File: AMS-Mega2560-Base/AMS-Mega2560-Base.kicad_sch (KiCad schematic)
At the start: 18 parts, among them J1 RTD1, J2 RTD2, J3 AdafruitUltimateGPS, J4 Sense, J5 Sense, P1 Power, P10 CONN_01X01, P11 CONN_01X01, P12 CONN_01X01, P13 CONN_01X01, P2 Analog, P3 Analog, P4 Digital, P5 PWM, P6 PWM, P7 Communication, P8 CONN_01X01, P9 CONN_01X01

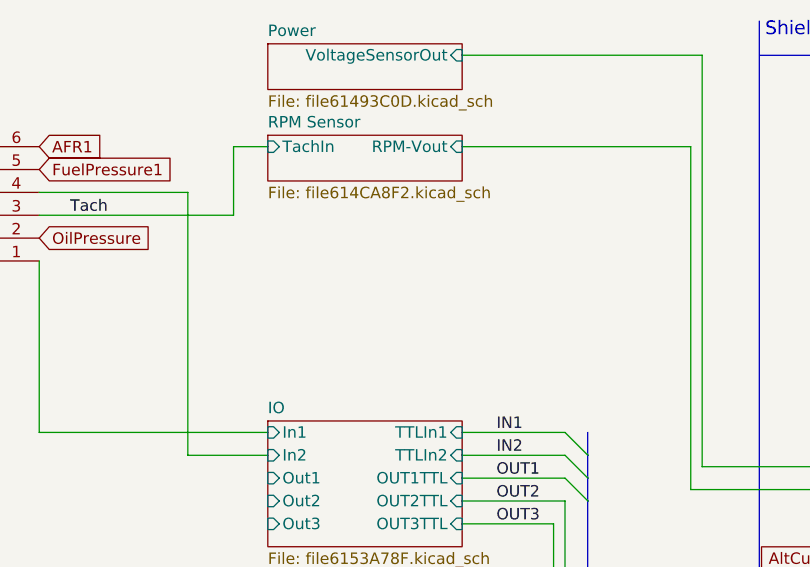
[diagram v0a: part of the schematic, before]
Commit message: fixing some library settings and updating some schematics
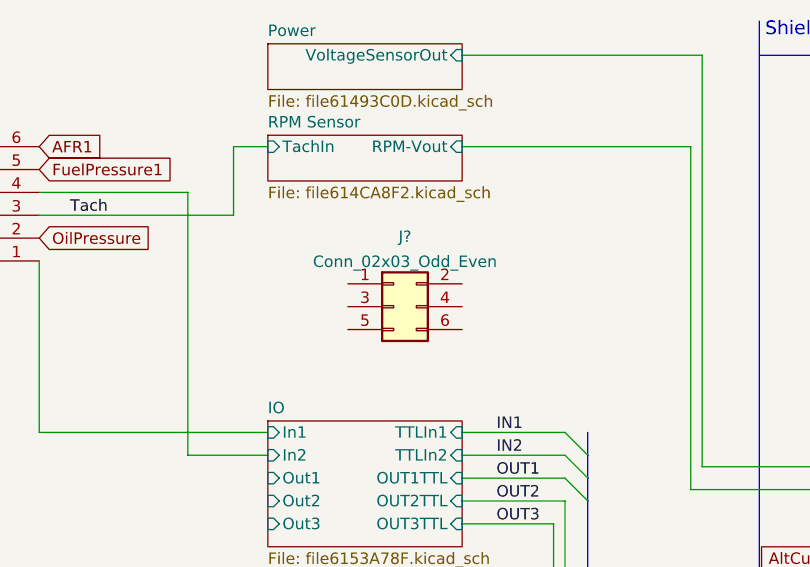
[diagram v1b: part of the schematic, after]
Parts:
- added J?: Conn_02x03_Odd_Even, Connector_PinHeader_2.54mm:PinHeader_2x03_P2.54mm_Vertical, symbol Connector_Generic:Conn_02x03_Odd_Even

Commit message: BaseBoard fixes and updates. doing schematic work.
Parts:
- removed J3: AdafruitUltimateGPS, Connector_PinSocket_2.54mm:PinSocket_1x09_P2.54mm_Vertical, symbol Connector_Generic:Conn_01x09
- gave numbers to parts that had none: 1
- renumbered J5 to J3
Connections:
- net 17(Rx2) is gone; now on net ComRX: P7.4 (Pin_4)
- net 50(MISO) is gone; now on net MISO: P4.5 (Pin_5)
- net 51(MOSI) is gone; now on net MOSI: P4.6 (Pin_6)
- net 52(SCK) is gone; now on net SCLK: P4.3 (Pin_3)
- net +5VP: no longer J3.9
- net GND: no longer J3.12
- net Inputs/In1: no longer J4.1
- net Inputs/In2: no longer J4.4
- net Sheet6152913C/RSCOM1RX: no longer J3.3
- net Sheet6152913C/RSCOM1TX: no longer J3.6
- net Vacuum1: now reaches P2.3 (Pin_3)
- net Vacuum2: now reaches P2.4 (Pin_4)
- net 16(Tx2) renamed ComTX
- net 2(**) renamed IN1
- net 3(**) renamed IN2
- net 34 renamed SDDetect
- net 36 renamed SDCS
- net 38 renamed CarbCS
- net 40 renamed AmbientCS
- net 42 renamed FrontCS
- net 44 renamed RsideCS
- net 45 renamed IN3
- net 46 renamed LsideCS
- net 47 renamed IN4
- net 48 renamed WaterCS
- net 49 renamed Logging
- net A0 renamed VoltageSensor
- net Sheet6152913C/AudioSiren: no longer names the net of J3.7
- net Sheet6152913C/Input1: no longer names the net of J3.11
- net Sheet6152913C/Input2: no longer names the net of J3.8
- net Sheet6152913C/LoggingSwitchIN: no longer names the net of J3.10
- net Tach: no longer names the net of J4.3
- no-connect marks 31 -> 27
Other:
- sheet IO renamed Inputs
- added sheet Outputs (Outputs.kicad_sch)
- sheet Inputs ports: added In3, In4, LoggingSwitchIN, TTLIn3, TTLIn4, TTLLoggingSwitch; removed OUT1TTL, OUT2TTL, OUT3TTL, Out1, Out2, Out3
- sheet Power ports: added none; removed VoltageSensorOut
- sheet Sheet6152913C ports: added none; removed AudioSiren, AudioSirenTTL, Input1, Input2, LED1, LED1TTL, LED2, LED2TTL, LoggingSwitchIN, TTLInput1, TTLInput2, TTLLoggingSwitch
- moved on the sheet: J1, J2, J3, J4, J5, P4

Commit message: trying to fix the PCB layout.
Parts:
- added J6: Conn_01x03, Connector_PinSocket_2.54mm:PinSocket_1x03_P2.54mm_Vertical, symbol Connector_Generic:Conn_01x09
- added J7: Conn_01x08, Connector_PinSocket_2.54mm:PinSocket_1x08_P2.54mm_Horizontal, symbol Connector_Generic:Conn_01x08
- added R1: 50K, Resistor_THT:R_Axial_DIN0207_L6.3mm_D2.5mm_P2.54mm_Vertical, symbol Device:R
- J3: renamed from J5; value Conn_02x03_Odd_Even -> Sense; footprint Connector_PinHeader_2.54mm:PinHeader_2x03_P2.54mm_Vertical -> SamacSys_Parts:1727751
- J4: value Sense -> Conn_02x03_Odd_Even; footprint SamacSys_Parts:1727751 -> Connector_PinHeader_2.54mm:PinHeader_2x03_P2.54mm_Vertical
- P1: value Power -> CONN_01X01; footprint Socket_Arduino_Mega:Socket_Strip_Arduino_1x08 -> Socket_Arduino_Mega:Arduino_1pin
- P2, P3: value Analog -> CONN_01X01; footprint Socket_Arduino_Mega:Socket_Strip_Arduino_1x08 -> Socket_Arduino_Mega:Arduino_1pin
- P4: value Digital -> CONN_01X01; footprint Socket_Arduino_Mega:Socket_Strip_Arduino_2x18 -> Socket_Arduino_Mega:Arduino_1pin
- P5: value PWM -> CONN_01X01; footprint Socket_Arduino_Mega:Socket_Strip_Arduino_1x10 -> Socket_Arduino_Mega:Arduino_1pin
- renumbered J3 to J5, P8 to P11, P9 to P12, P10 to P13, P11 to P14, P12 to P15, P13 to P16
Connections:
- net +10V: now also J3.2 (Pin_2)
- net +5VP: now also J3.1 (Pin_1), J6.8 (Pin_8), J7.1 (Pin_1), R1.1
- net GND: now also J3.6 (Pin_6), J6.7 (Pin_7), J7.3 (Pin_3)
- net GPSBat: now also J6.3 (Pin_3)
- net GPSRX: now also J6.6 (Pin_6)
- net GPSTX: now also J6.5 (Pin_5)
- net MISO: now also J7.5 (Pin_5)
- net MOSI: now also J7.6 (Pin_6)
- net SCLK: now also J7.4 (Pin_4)
- net SDCS: now also J7.7 (Pin_7)
- net SDDetect: now also J7.8 (Pin_8), R1.2
- net Vacuum1: now also J3.3 (Pin_3)
- net Vacuum2: now also J3.5 (Pin_5)
- net Sense1-1: now reaches J4.1
- net Sense1-10: now reaches J4.10
- net Sense1-11: now reaches J4.11
- net Sense1-3: now reaches J4.3
- net Sense1-4: now reaches J4.4
- net Sense1-7: now reaches J4.7
- net Sense2-1: now reaches J5.1
- net Sense2-10: now reaches J5.10
- net Sense2-11: now reaches J5.11
- net Sense2-12: now reaches J5.12
- net Sense2-3: now reaches J5.3
- net Sense2-4: now reaches J5.4
- net Sense2-6: now reaches J5.6
- net Sense2-7: now reaches J5.7
- net Sense2-8: now reaches J5.8
- net Sense2-9: now reaches J5.9
- net +2V5: now reaches J3.4 (Pin_4)
- net 4(**) renamed OUTPUT1
- net 41 renamed OUTPUTLED1
- net 43 renamed OUTPUTLED2
- net 5(**) renamed OUTPUT2
- net 6(**) renamed OUTPUT3
- net 7(**) renamed OUTPUT4
- net 8(**) renamed OUTPUTSiren
- new net 3.3: J6.1 (Pin_1)
- new net EN: J6.2 (Pin_2)
- new net FIX: J6.4 (Pin_4)
- new net PPS: J6.9 (Pin_9)
- no-connect marks 27 -> 28
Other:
- sheet 3.3 Logic Convert ports: added none; removed 5VSDCS, SDDetect
- note added: "GPS Board Connection"
- note added: "Inputs/Outputs"
- note added: "SD Board Connection"
- note added: "Terminal Blocks"
- note added: "Terminal Blocks, RTD and Level Shifting"
- note added: "Vacuum Board Connections"
- moved on the sheet: J1, J2, J3, J4, J5, P1, P11, P12, P13, P14, P15, P16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

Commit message: rollback and file clean up.
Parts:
- removed J6: Conn_01x03, Connector_PinSocket_2.54mm:PinSocket_1x03_P2.54mm_Vertical, symbol Connector_Generic:Conn_01x09
- removed J7: Conn_01x08, Connector_PinSocket_2.54mm:PinSocket_1x08_P2.54mm_Horizontal, symbol Connector_Generic:Conn_01x08
- removed R1: 50K, Resistor_THT:R_Axial_DIN0207_L6.3mm_D2.5mm_P2.54mm_Vertical, symbol Device:R
- J3: renamed from J4; value Conn_02x03_Odd_Even -> Sense; footprint Connector_PinHeader_2.54mm:PinHeader_2x03_P2.54mm_Vertical -> SamacSys_Parts:1727751
- J4: renamed from J3; value Sense -> Conn_02x03_Odd_Even; footprint SamacSys_Parts:1727751 -> Connector_PinHeader_2.54mm:PinHeader_2x03_P2.54mm_Vertical
- P1: value CONN_01X01 -> Power; footprint Socket_Arduino_Mega:Arduino_1pin -> Socket_Arduino_Mega:Socket_Strip_Arduino_1x08
- P2, P3: value CONN_01X01 -> Analog; footprint Socket_Arduino_Mega:Arduino_1pin -> Socket_Arduino_Mega:Socket_Strip_Arduino_1x08
- P4: value CONN_01X01 -> Digital; footprint Socket_Arduino_Mega:Arduino_1pin -> Socket_Arduino_Mega:Socket_Strip_Arduino_2x18
- P5: value CONN_01X01 -> PWM; footprint Socket_Arduino_Mega:Arduino_1pin -> Socket_Arduino_Mega:Socket_Strip_Arduino_1x10
- renumbered P13 to P10, P14 to P11, P15 to P12, P16 to P13, P11 to P8, P12 to P9
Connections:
- net +10V: no longer J4.2 (Pin_2)
- net +2V5: no longer J4.4 (Pin_4)
- net +5VP: no longer J4.1 (Pin_1)
- net GND: no longer J4.6 (Pin_6)
- net Vacuum1: no longer J4.3 (Pin_3)
- net Vacuum2: no longer J4.5 (Pin_5)
- no-connect marks 28 -> 23
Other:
- sheet 3.3 Logic Convert ports: added 5VSDCS, SDDetect; removed none
- note removed: "GPS Board Connection"
- note removed: "Inputs/Outputs"
- note removed: "SD Board Connection"
- note removed: "Terminal Blocks"
- note removed: "Terminal Blocks, RTD and Level Shifting"
- note removed: "Vacuum Board Connections"
- moved on the sheet: J1, J2, J3, J4, J5, P1, P10, P11, P12, P13, P2, P3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

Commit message: fixed the messed up references and cleaned up the schematic.
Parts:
- added J3: Conn_01x08, Connector_PinSocket_2.54mm:PinSocket_1x08_P2.54mm_Horizontal, symbol Connector_Generic:Conn_01x08
- added J6: AdafruitUltimateGPS, Connector_PinSocket_2.54mm:PinSocket_1x09_P2.54mm_Vertical, symbol Connector_Generic:Conn_01x09
- added R1: 50K, Resistor_THT:R_Axial_DIN0207_L6.3mm_D2.5mm_P2.54mm_Vertical, symbol Device:R
- J4: renamed from J3; value Sense -> Sense1
- J5: value Sense -> Sense2
- renumbered J4 to J7
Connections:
- net +10V: now also J7.2 (Pin_2)
- net +2V5: now also J7.4 (Pin_4)
- net +5VP: now also J7.1 (Pin_1), J3.1 (Pin_1), J6.8 (Pin_8), R1.1
- net GND: now also J7.6 (Pin_6), J3.3 (Pin_3), J6.7 (Pin_7)
- net GPSBat: now also J6.3 (Pin_3)
- net GPSRX: now also J6.6 (Pin_6)
- net GPSTX: now also J6.5 (Pin_5)
- net MISO: now also J3.5 (Pin_5)
- net MOSI: now also J3.6 (Pin_6)
- net SCLK: now also J3.4 (Pin_4)
- net SDCS: now also J3.7 (Pin_7)
- net SDDetect: now also J3.8 (Pin_8), R1.2
- net Vacuum1: now also J7.3 (Pin_3)
- net Vacuum2: now also J7.5 (Pin_5)
- new net 3.3: J6.1 (Pin_1)
- new net EN: J6.2 (Pin_2)
- new net FIX: J6.4 (Pin_4)
- new net PPS: J6.9 (Pin_9)
- no-connect marks 23 -> 28
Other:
- sheet 3.3 Logic Convert ports: added none; removed 5VSDCS, SDDetect
- note added: "GPS Connection"
- note added: "Inputs/Outputs"
- note added: "SD Card Connection"
- note added: "Terminal Blocks"
- note added: "Vaccum Sensor Connections"
- moved on the sheet: J1, J2, J4, J5, J7, P1, P10, P11, P12, P13, P2, P3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

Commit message: working on pcb layout
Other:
- note added: "Inputs"
- note added: "Outputs"
- note added: "Power"
- note removed: "Inputs/Outputs"

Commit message: wip for the base PCB, finished Vacuum PCB and Fab Files for that.
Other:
- note added: "RTD and level Shifters"
- moved on the sheet: J4, J5

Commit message: WIP for layout
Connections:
- net Com3.3RX renamed 19(Rx1)
- net Com3.3TX renamed 18(Tx1)
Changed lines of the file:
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@@
+    )
+  )
+  (global_label "ComRX" (shape input) (at 140.97 275.59 0) (fields_autoplaced)
+    (effects (font (size 1.27 1.27)) (justify left))
+    (property "Intersheet References" "${INTERSHEET_REFS}" (id 0) (at -134.62 181.61 0)
+      (effects (font (size 1.27 1.27)) hide)
     )
   )
@@
     )
   )
-  (global_label "Com3.3TX" (shape input) (at 140.97 278.13 0) (fields_autoplaced)
-    (effects (font (size 1.27 1.27)) (justify left))
-    (property "Intersheet References" "${INTERSHEET_REFS}" (id 0) (at -5.08 83.82 0)
-      (effects (font (size 1.27 1.27)) hide)
-    )
-  )
   (global_label "FuelPressure1" (shape input) (at 341.63 74.93 180) (fields_autoplaced)
     (effects (font (size 1.27 1.27)) (justify right))
@@
     )
   )
-  (global_label "Com3.3RX" (shape input) (at 393.7 99.06 0) (fields_autoplaced)
-    (effects (font (size 1.27 1.27)) (justify left))
-    (property "Intersheet References" "${INTERSHEET_REFS}" (id 0) (at 118.11 0 0)
-      (effects (font (size 1.27 1.27)) hide)
-    )
-  )
   (global_label "IN4" (shape input) (at 354.33 152.4 270) (fields_autoplaced)
     (effects (font (size 1.27 1.27)) (justify right))
@@
     )
   )
-  (global_label "Com3.3TX" (shape input) (at 393.7 96.52 0) (fields_autoplaced)
-    (effects (font (size 1.27 1.27)) (justify left))
-    (property "Intersheet References" "${INTERSHEET_REFS}" (id 0) (at 118.11 0 0)
-      (effects (font (size 1.27 1.27)) hide)
-    )
-  )
   (global_label "ComTX" (shape input) (at 393.7 91.44 0) (fields_autoplaced)
     (effects (font (size 1.27 1.27)) (justify left))
@@
     )
   )
-  (global_label "Com3.3RX" (shape input) (at 140.97 275.59 0) (fields_autoplaced)
-    (effects (font (size 1.27 1.27)) (justify left))
-    (property "Intersheet References" "${INTERSHEET_REFS}" (id 0) (at -5.08 83.82 0)
-      (effects (font (size 1.27 1.27)) hide)
-    )
-  )
   (global_label "Sense2-12" (shape input) (at 31.75 57.15 180) (fields_autoplaced)
     (effects (font (size 1.27 1.27)) (justify right))
@@
     )
   )
+  (global_label "ComTX" (shape input) (at 140.97 278.13 0) (fields_autoplaced)
+    (effects (font (size 1.27 1.27)) (justify left))
+    (property "Intersheet References" "${INTERSHEET_REFS}" (id 0) (at -134.62 186.69 0)
+      (effects (font (size 1.27 1.27)) hide)
+    )
+  )
